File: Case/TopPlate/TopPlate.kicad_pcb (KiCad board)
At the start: 2 copper layers, 136.5 x 87.7 mm, 33 parts

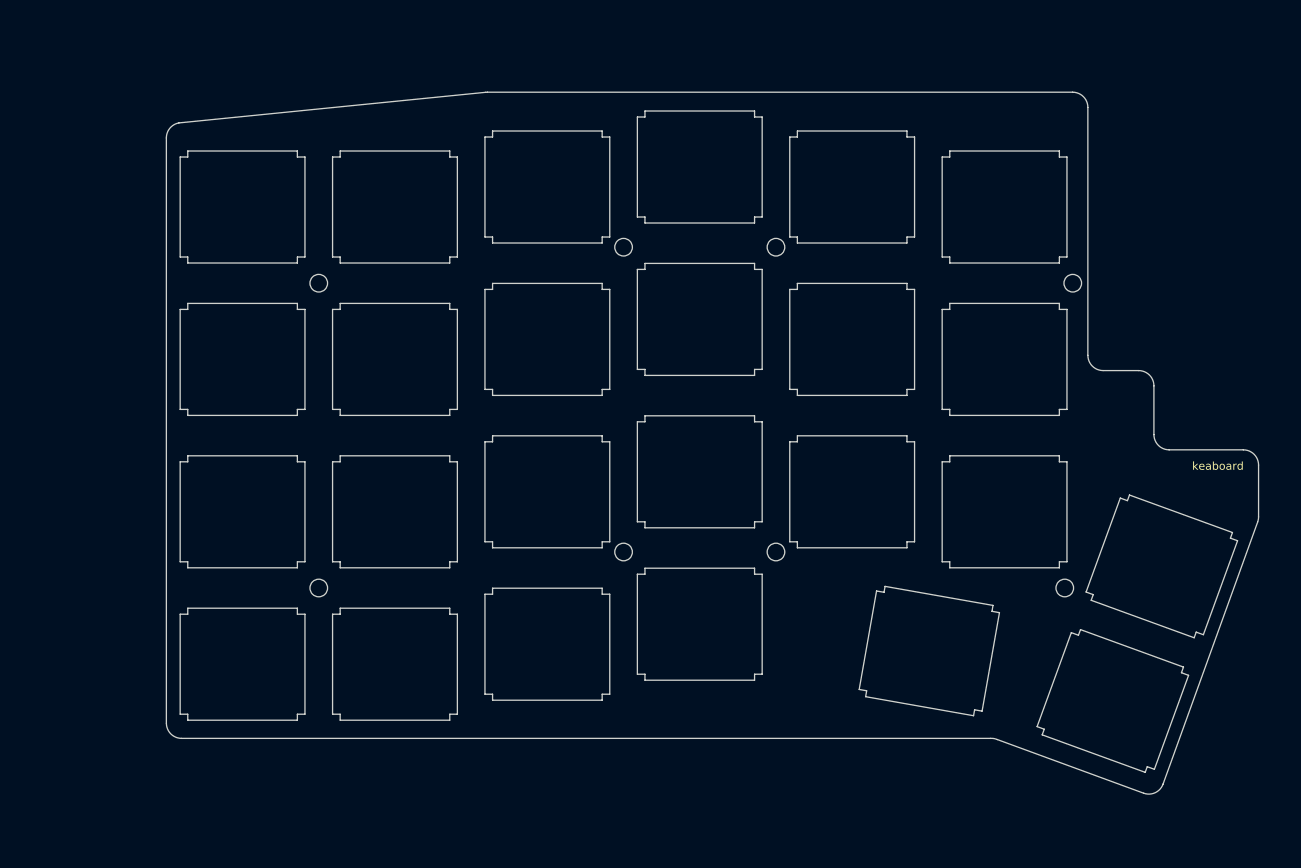
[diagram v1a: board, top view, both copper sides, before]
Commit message: Resize PCB to add more space around the edges to avoid breaking parts, update images, update gerber
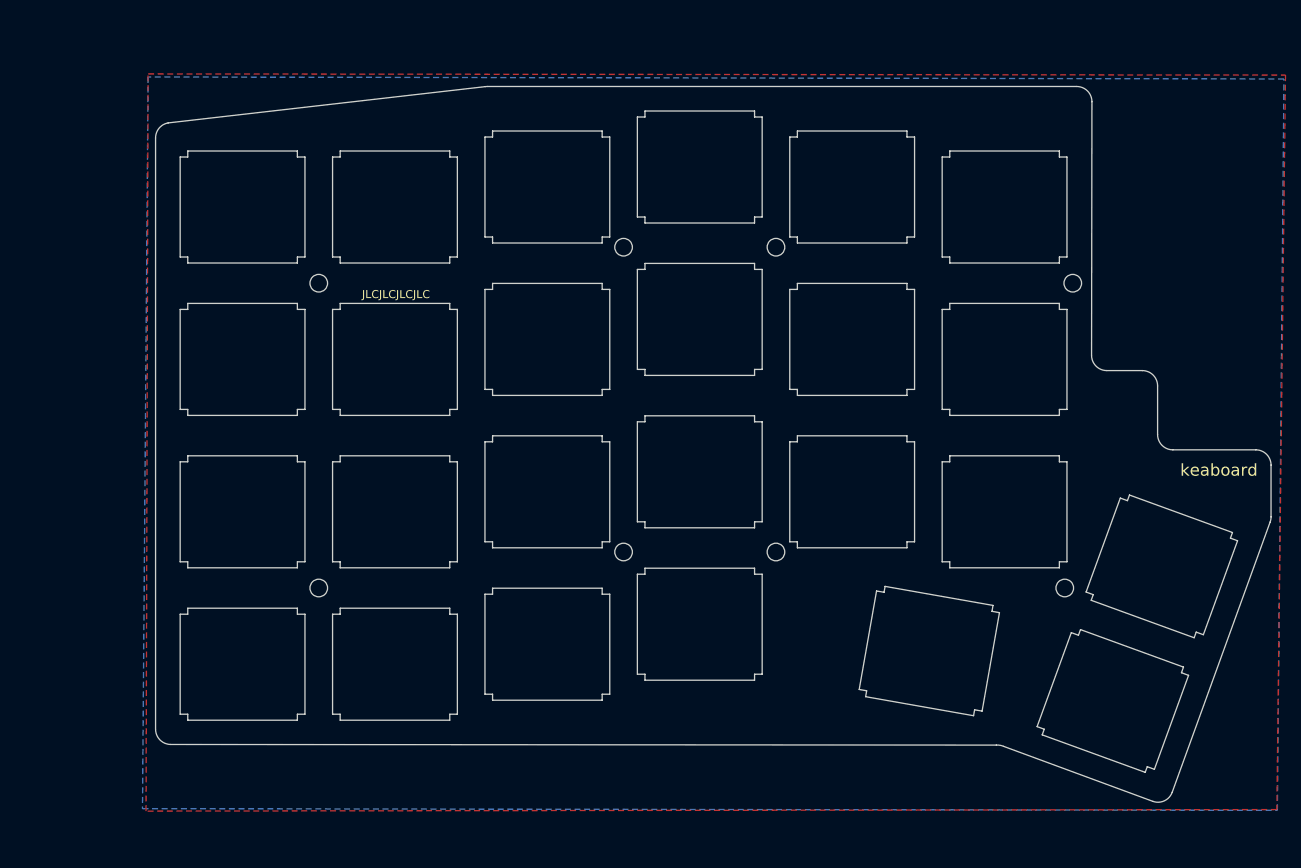
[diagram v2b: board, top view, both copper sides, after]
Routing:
- added copper zone on B.Cu, net (none)
- added copper zone on F.Cu, net (none)
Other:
- board size 136.5 x 87.7 mm -> 139.4 x 89.5 mm
- board text added: "JLCJLCJLCJLC"
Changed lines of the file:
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@@
   (general
     (thickness 1.6)
-    (drawings 24)
+    (drawings 25)
     (tracks 0)
     (zones 0)
@@
     (38 B.Mask user)
     (39 F.Mask user)
-    (40 Dwgs.User user hide)
-    (41 Cmts.User user hide)
-    (42 Eco1.User user hide)
+    (40 Dwgs.User user)
+    (41 Cmts.User user)
+    (42 Eco1.User user)
     (43 Eco2.User user)
     (44 Edge.Cuts user)
-    (45 Margin user hide)
-    (46 B.CrtYd user hide)
-    (47 F.CrtYd user hide)
-    (48 B.Fab user hide)
-    (49 F.Fab user hide)
+    (45 Margin user)
+    (46 B.CrtYd user)
+    (47 F.CrtYd user)
+    (48 B.Fab user)
+    (49 F.Fab user)
   )
   (setup
@@
     (visible_elements FFFFFF7F)
     (pcbplotparams
-      (layerselection 0x010f0_ffffffff)
+      (layerselection 0x010fc_ffffffff)
       (usegerberextensions false)
       (usegerberattributes true)
@@
     (pad 1 np_thru_hole circle (at 0 0) (size 2.2 2.2) (drill 2.2) (layers *.Cu *.Mask))
   )
-  (gr_arc (start 166.37 69.977) (end 168.275 69.977) (angle -90) (layer Edge.Cuts) (width 0.1))
-  (gr_line (start 161.925 68.072) (end 166.37 68.072) (layer Edge.Cuts) (width 0.1))
-  (gr_arc (start 170.18 76.073) (end 168.275 76.073) (angle -90) (layer Edge.Cuts) (width 0.1))
-  (gr_arc (start 161.925 66.167) (end 160.02 66.167) (angle -90) (layer Edge.Cuts) (width 0.1))
-  (gr_line (start 168.275 69.977) (end 168.275 76.073) (layer Edge.Cuts) (width 0.1))
-  (gr_text keaboard (at 176.276 80.01) (layer B.SilkS)
-    (effects (font (size 1 1) (thickness 0.2)) (justify mirror))
-  )
-  (gr_text keaboard (at 176.276 80.01) (layer F.SilkS)
+  (gr_text JLCJLCJLCJLC (at 73.533 58.547) (layer F.SilkS)
     (effects (font (size 1 1) (thickness 0.2)))
   )
-  (gr_line (start 160.02 35.179) (end 160.02 66.167) (layer Edge.Cuts) (width 0.1))
-  (gr_line (start 170.18 77.978) (end 179.451 77.978) (layer Edge.Cuts) (width 0.1))
-  (gr_arc (start 179.451 79.883) (end 181.356 79.883) (angle -90) (layer Edge.Cuts) (width 0.1))
-  (gr_arc (start 158.115 35.179) (end 160.02 35.179) (angle -90) (layer Edge.Cuts) (width 0.1))
-  (gr_line (start 44.831 112.141) (end 44.831 38.989) (layer Edge.Cuts) (width 0.1))
-  (gr_line (start 147.828 114.046) (end 46.736 114.046) (layer Edge.Cuts) (width 0.1))
-  (gr_arc (start 46.736 112.141) (end 44.831 112.141) (angle -90) (layer Edge.Cuts) (width 0.1))
-  (gr_arc (start 147.954728 115.976249) (end 148.716727 114.19825) (angle -26.95486857) (layer Edge.Cuts) (width 0.1))
-  (gr_line (start 46.4052 37.112941) (end 84.711228 33.290711) (layer Edge.Cuts) (width 0.1))
-  (gr_line (start 167.005002 120.903998) (end 148.716727 114.19825) (layer Edge.Cuts) (width 0.1))
-  (gr_arc (start 84.963 35.179) (end 84.963 33.274) (angle -7.594647344) (layer Edge.Cuts) (width 0.1))
-  (gr_line (start 181.24601 86.995) (end 169.418 119.761) (layer Edge.Cuts) (width 0.1))
-  (gr_line (start 84.963 33.274001) (end 158.115 33.274) (layer Edge.Cuts) (width 0.1))
-  (gr_line (start 181.356 79.883) (end 181.356 86.36) (layer Edge.Cuts) (width 0.1))
-  (gr_arc (start 179.46801 86.360001) (end 181.24601 86.995) (angle -19.65382589) (layer Edge.Cuts) (width 0.1))
-  (gr_arc (start 46.736 38.989) (end 44.831 38.989) (angle 80) (layer Edge.Cuts) (width 0.1))
-  (gr_arc (start 167.64 119.126) (end 167.005002 120.903998) (angle -90) (layer Edge.Cuts) (width 0.1))
+  (gr_text keaboard (at 176.403 80.518) (layer B.SilkS)
+    (effects (font (size 1.5 1.5) (thickness 0.2)) (justify mirror))
+  )
+  (gr_arc (start 166.83 69.977) (end 168.735 69.977) (angle -90) (layer Edge.Cuts) (width 0.1))
+  (gr_line (start 162.385 68.072) (end 166.83 68.072) (layer Edge.Cuts) (width 0.1))
+  (gr_arc (start 170.64 76.073) (end 168.735 76.073) (angle -90) (layer Edge.Cuts) (width 0.1))
+  (gr_arc (start 162.385 66.167) (end 160.48 66.167) (angle -90) (layer Edge.Cuts) (width 0.1))
+  (gr_line (start 168.735 69.977) (end 168.735 76.073) (layer Edge.Cuts) (width 0.1))
+  (gr_text keaboard (at 176.403 80.518) (layer F.SilkS)
+    (effects (font (size 1.5 1.5) (thickness 0.2)))
+  )
+  (gr_line (start 160.528 34.465) (end 160.48 66.167) (layer Edge.Cuts) (width 0.1))
+  (gr_line (start 170.64 77.978) (end 181.011 77.978) (layer Edge.Cuts) (width 0.1))
+  (gr_arc (start 181.011 79.883) (end 182.916 79.883) (angle -90) (layer Edge.Cuts) (width 0.1))
+  (gr_arc (start 158.623 34.465) (end 160.528 34.465) (angle -90) (layer Edge.Cuts) (width 0.1))
+  (gr_line (start 43.482 112.903) (end 43.482 38.989) (layer Edge.Cuts) (width 0.1))
+  (gr_line (start 148.590273 114.887) (end 45.387 114.808) (layer Edge.Cuts) (width 0.1))
+  (gr_arc (start 45.387 112.903) (end 43.482 112.903) (angle -90) (layer Edge.Cuts) (width 0.1))
+  (gr_arc (start 148.717001 116.817249) (end 149.479 115.03925) (angle -26.95486857) (layer Edge.Cuts) (width 0.1))
+  (gr_line (start 45.0562 37.112941) (end 84.711228 32.576711) (layer Edge.Cuts) (width 0.1))
+  (gr_line (start 168.148 121.92) (end 149.479 115.03925) (layer Edge.Cuts) (width 0.1))
+  (gr_arc (start 84.963 34.465) (end 84.963 32.56) (angle -7.594647344) (layer Edge.Cuts) (width 0.1))
+  (gr_line (start 182.80601 86.995) (end 170.560996 120.777) (layer Edge.Cuts) (width 0.1))
+  (gr_line (start 84.963 32.56) (end 158.623 32.56) (layer Edge.Cuts) (width 0.1))
+  (gr_line (start 182.916 79.883) (end 182.916 86.36) (layer Edge.Cuts) (width 0.1))
+  (gr_arc (start 181.02801 86.360001) (end 182.80601 86.995) (angle -19.65382589) (layer Edge.Cuts) (width 0.1))
+  (gr_arc (start 45.387 38.989) (end 43.482 38.989) (angle 80) (layer Edge.Cuts) (width 0.1))
+  (gr_arc (start 168.782998 120.142002) (end 168.148 121.92) (angle -90) (layer Edge.Cuts) (width 0.1))
+  (zone (net 0) (net_name "") (layer F.Cu) (hatch edge 0.508)
+    (connect_pads (clearance 0.508))
+    (min_thickness 0.254)
+    (fill yes (arc_segments 32) (thermal_gap 0.508) (thermal_bridge_width 0.508))
+    (polygon
+      (pts
+        (xy 183.642 122.943938) (xy 42.291 123.138407) (xy 42.545 30.988) (xy 184.7215 31.136828)
+      )
+    )
+  )
+  (zone (net 0) (net_name "") (layer B.Cu) (hatch edge 0.508)
+    (connect_pads (clearance 0.508))
+    (min_thickness 0.254)
+    (fill yes (arc_segments 32) (thermal_gap 0.508) (thermal_bridge_width 0.508))
+    (polygon
+      (pts
+        (xy 184.531 31.623) (xy 42.545 31.369) (xy 41.8465 122.830828) (xy 183.7055 123.041172)
+      )
+    )
+  )
 )

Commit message: Update cases, update edge cuts on main pcb, start routing traces to controller
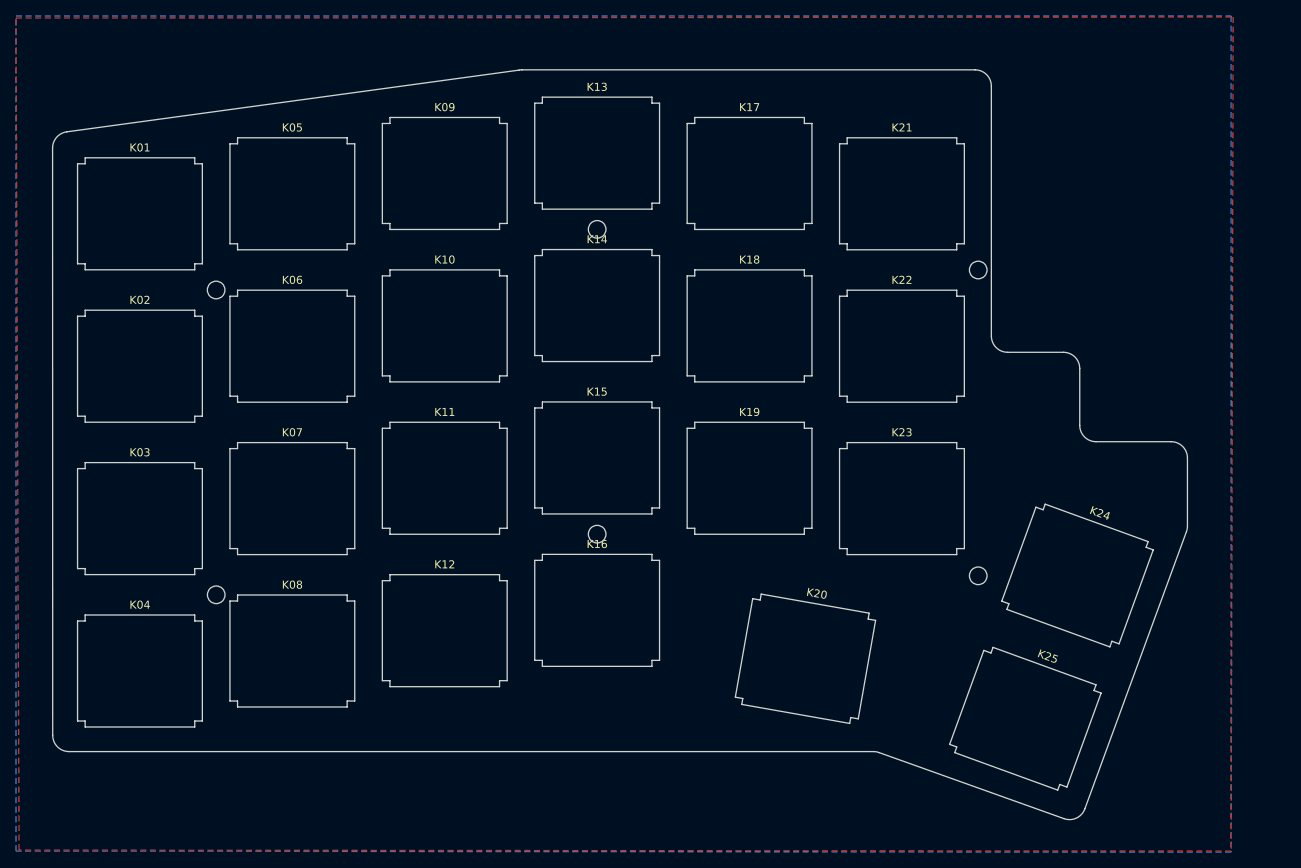
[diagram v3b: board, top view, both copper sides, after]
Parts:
- removed the REF** at (163.1, 109.4)
- removed the REF** at (111.5, 80.7)
- removed the REF** at (111.5, 99.8)
- removed the REF** at (111.5, 42.6)
- removed the REF** at (111.5, 61.7)
- removed the REF** at (73.4, 66.7)
- removed the REF** at (73.4, 85.7)
- removed the REF** at (73.4, 104.8)
- removed the REF** at (73.4, 47.6)
- removed the REF** at (92.5, 45.1)
- removed the REF** at (92.5, 64.2)
- removed the REF** at (169.3, 92.5)
- removed the REF** at (92.5, 102.3)
- removed the REF** at (92.5, 83.2)
- removed the REF** at (54.4, 47.6)
- removed the REF** at (54.4, 66.7)
- removed the REF** at (54.4, 85.7)
- removed the REF** at (54.4, 104.8)
- removed the REF** at (63.9, 95.2)
- removed the REF** at (102.0, 90.8)
- removed the REF** at (157.1, 95.2)
- removed the REF** at (102.0, 52.6)
- removed the REF** at (140.2, 103.1)
- removed the REF** at (121.0, 52.6)
- removed the REF** at (63.9, 57.1)
- removed the REF** at (158.1, 57.1)
- removed the REF** at (121.0, 90.8)
- removed the REF** at (149.6, 66.7)
- removed the REF** at (130.6, 83.2)
- removed the REF** at (149.6, 47.6)
- removed the REF** at (130.6, 64.2)
- removed the REF** at (130.6, 45.1)
- removed the REF** at (149.6, 85.7)
- added K01: KEYSW, parts:MX-Alps_Switch_Cutout_simple, B.Cu at (41.5, 48.5)
- added K02: KEYSW, parts:MX-Alps_Switch_Cutout_simple, B.Cu at (41.5, 67.5)
- added K03: KEYSW, parts:MX-Alps_Switch_Cutout_simple, B.Cu at (41.5, 86.6)
- added K04: KEYSW, parts:MX-Alps_Switch_Cutout_simple, B.Cu at (41.5, 105.6)
- added K05: KEYSW, parts:MX-Alps_Switch_Cutout_simple, B.Cu at (60.6, 46.0)
- added K06: KEYSW, parts:MX-Alps_Switch_Cutout_simple, B.Cu at (60.6, 65.0)
- added K07: KEYSW, parts:MX-Alps_Switch_Cutout_simple, B.Cu at (60.6, 84.1)
- added K08: KEYSW, parts:MX-Alps_Switch_Cutout_simple, B.Cu at (60.6, 103.1)
- added K09: KEYSW, parts:MX-Alps_Switch_Cutout_simple, B.Cu at (79.6, 43.4)
- added K10: KEYSW, parts:MX-Alps_Switch_Cutout_simple, B.Cu at (79.6, 62.5)
- added K11: KEYSW, parts:MX-Alps_Switch_Cutout_simple, B.Cu at (79.6, 81.5)
- added K12: KEYSW, parts:MX-Alps_Switch_Cutout_simple, B.Cu at (79.6, 100.6)
- added K13: KEYSW, parts:MX-Alps_Switch_Cutout_simple, B.Cu at (98.7, 40.9)
- added K14: KEYSW, parts:MX-Alps_Switch_Cutout_simple, B.Cu at (98.7, 59.9)
- added K15: KEYSW, parts:MX-Alps_Switch_Cutout_simple, B.Cu at (98.7, 79.0)
- added K16: KEYSW, parts:MX-Alps_Switch_Cutout_simple, B.Cu at (98.7, 98.0)
- added K17: KEYSW, parts:MX-Alps_Switch_Cutout_simple, B.Cu at (117.7, 43.4)
- added K18: KEYSW, parts:MX-Alps_Switch_Cutout_simple, B.Cu at (117.7, 62.5)
- added K19: KEYSW, parts:MX-Alps_Switch_Cutout_simple, B.Cu at (117.7, 81.5)
- added K20: KEYSW, parts:MX-Alps_Switch_Cutout_simple, B.Cu at (124.7, 104.1)
- added K21: KEYSW, parts:MX-Alps_Switch_Cutout_simple, B.Cu at (136.8, 46.0)
- added K22: KEYSW, parts:MX-Alps_Switch_Cutout_simple, B.Cu at (136.8, 65.0)
- added K23: KEYSW, parts:MX-Alps_Switch_Cutout_simple, B.Cu at (136.8, 84.1)
- added K24: KEYSW, parts:MX-Alps_Switch_Cutout_simple, B.Cu at (158.7, 93.7)
- added K25: KEYSW, parts:MX-Alps_Switch_Cutout_simple, B.Cu at (152.2, 111.6)
- added REF**: MountingHole_2.2mm_M2, MountingHole:MountingHole_2.2mm_M2, F.Cu at (51.1, 96.1)
- added REF**: MountingHole_2.2mm_M2, MountingHole:MountingHole_2.2mm_M2, F.Cu at (51.1, 58.0)
- added REF**: MountingHole_2.2mm_M2, MountingHole:MountingHole_2.2mm_M2, F.Cu at (98.7, 50.4)
- added REF**: MountingHole_2.2mm_M2, MountingHole:MountingHole_2.2mm_M2, F.Cu at (98.7, 88.5)
- added REF**: MountingHole_2.2mm_M2, MountingHole:MountingHole_2.2mm_M2, F.Cu at (146.3, 93.7)
- added REF**: MountingHole_2.2mm_M2, MountingHole:MountingHole_2.2mm_M2, F.Cu at (146.3, 55.5)
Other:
- board size 139.4 x 89.5 mm -> 141.9 x 93.7 mm
- board text removed: "JLCJLCJLCJLC"
- board text removed: "keaboard"

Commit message: Route traces, add labels
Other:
- board text added: "JLCJLCJLCJLC"
- board text added: "keaboard"
